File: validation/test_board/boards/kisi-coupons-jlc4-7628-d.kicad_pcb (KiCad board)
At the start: 4 copper layers, 50 x 96 mm, 19 parts, among them J1 292-04A-14, J10 292-04A-14, J11 292-04A-14, J12 292-04A-14, J13 292-04A-14, J14 292-04A-14, J15 292-04A-14, J16 292-04A-14, J2 292-04A-14, J3 292-04A-14, J4 292-04A-14, J5 292-04A-14, J6 292-04A-14, J7 292-04A-14, J8 292-04A-14, J9 292-04A-14

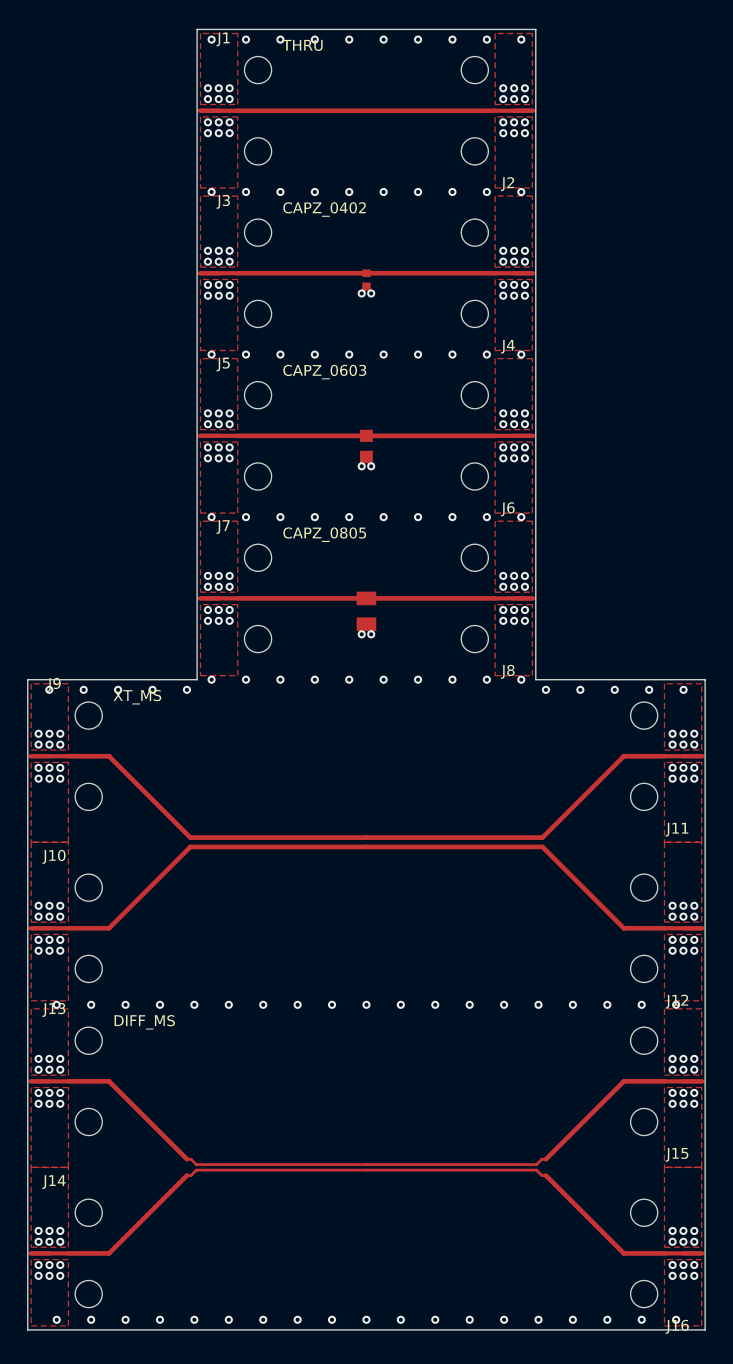
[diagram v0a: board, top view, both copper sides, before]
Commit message: Measurement coupons v3: Samtec 2.92 mm edge launch, 40 GHz plan
- Connector: Samtec 292-J-P-EP-ST-EL-01 (2.92 mm to 40 GHz, compression
  mount, PCB 1.02-2.54 mm; maintainer's decision 2026-10-30 on the RF
  group's advice) replaces the SMA Southwest 292-04A-14. Data, sources,
  the meaning of every footprint dimension of Samtec's drawing and the
  benchmark of Samtec's RF report (2023-06-01) in connectors.json.
- Footprint generated by make_coupons.py from parameters (Samtec's
  files are not committed: their terms forbid redistributing the
  models): geometry from drawing 292-J-P-EP-ST-EL-01-X-MKT rev C,
  plated screw holes 2.79 mm from the edge, +-2.92 mm, ground pads on
  top and bottom copper, signal tip 0.23 mm; marked DRAFT. The
  generator checks that no other net lies under the pads.
- Launch parametric (tip, taper, pad, coplanar section, ground cut,
  fence); default our 50 ohm coplanar launch inside the Samtec pads.
  --launch-cases writes kisi-fdtd cases; first runs (board side only)
  in fdtd_ref/launch_jlc4_7628: -18.9 dB worst to 40 GHz with the
  launch width to the edge, Samtec's 0.52 mm pad -14.6 dB.
- 40 GHz plan: stub notches of 6-layer VLV_L3 and 8-layer VLV_L6 now in
  the band, row via walls 2.54 -> 1.27 mm, measurement plan and ordering
  checklist to 40 GHz with 2.92 mm calibration and tools.
- Boards, manifests and 3D cases regenerated (widths unchanged); DRC
  with KiCad 7 on converted copies: no errors; kisi check rerun with
  kisi 0.3.1 (three v2 findings resolved in kisi since).

Co-Authored-By: Claude Opus 5.5 <noreply@anthropic.com>
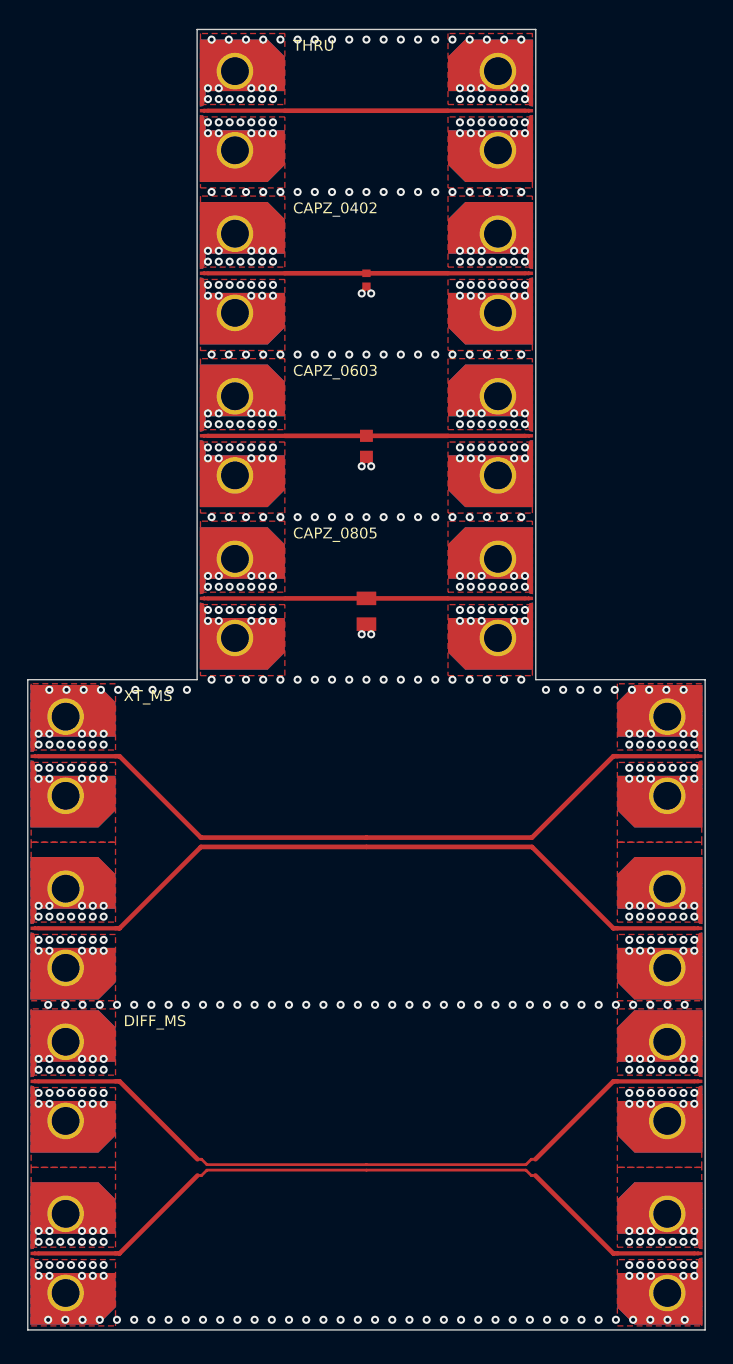
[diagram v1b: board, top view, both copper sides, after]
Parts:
- removed the J12 at (80.0, 96.3)
- added C1: 100nF 16V X7R, Capacitor_SMD:C_0402_1005Metric, F.Cu at (55.0, 48.5)
- J1, J10, J11, J13, J14, J15, J16, J2, J3, J4, J5, J6, J7, J8, J9: value 292-04A-14 -> 292-J-P-EP-ST-EL-01; footprint kisi_coupons:SWM_292-04A-14_EndLaunch_PLACEHOLDER -> kisi_coupons:Samtec_292-J-P-EP-ST-EL-01_EdgeLaunch
- J12: renamed from C1; value 100nF 16V X7R -> 292-J-P-EP-ST-EL-01; footprint Capacitor_SMD:C_0402_1005Metric -> kisi_coupons:Samtec_292-J-P-EP-ST-EL-01_EdgeLaunch
- moved J12 54.0 mm to (80.0, 96.3), turned to 180 degrees
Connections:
- J12 pad 1: SE_CAPZ_0402 -> SE_XT_V
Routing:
- net DP_DIFF_MS_P: track 54.7 -> 53.5 mm
- net DP_DIFF_MS_N: track 54.7 -> 53.5 mm
- net SE_XT_V: track 54.6 -> 53.4 mm
- net SE_XT_A: track 54.6 -> 53.4 mm
- net SE_THRU: track 24.6 -> 23.4 mm
- net SE_CAPZ_0805: track 24.6 -> 23.4 mm
- net SE_CAPZ_0603: track 24.6 -> 23.4 mm
- net SE_CAPZ_0402: track 24.6 -> 23.4 mm
- net GND: vias 296 -> 579
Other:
- board text added: "2026-10-30"
- board text added: "Connector footprint generated from Samtec's drawing (DRAFT, connectors.json); launch not yet optimised."
- board text added: "Copper comes to 0.2 mm from the left/right edges at the 2.92 mm edge launches (Samtec 292-J-P-EP-ST-EL-01, plated screw holes)."
- board text added: "JLC04161H-7628 v3"
- board text added: "kisi-coupons-jlc4-7628-d: kisi measurement coupons v3 (2026-10-30)"
- board text removed: "Connector footprint is a PLACEHOLDER (connectors.json) until the vendor drawing is supplied."
- board text removed: "Copper comes to 0.2 mm from the left/right edges at the SMA end launches (Southwest Microwave 292-04A-14)."
- board text removed: "JLC04161H-7628 v2 2026-10-22"
- board text removed: "kisi-coupons-jlc4-7628-d: kisi measurement coupons v2 (2026-10-22)"

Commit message: Launch optimisation step 1: launch width to the edge, fence 0.55 mm
- kisi-fdtd launch cases on the 7628 stack, board side (the connector's
  coax not modelled): our 50 ohm coplanar launch run to the edge with a
  0.55 mm fence from 0.5 mm gives |S11| -21.0 dB at worst to 40 GHz;
  the 0.8 mm draft fence left |S21| dips at 25-38 GHz (-18.9 dB),
  Samtec's 0.23 mm tip -15.7 dB (-16.8 dB with the pin modelled), its
  0.52 mm pad -14.6 dB. These become the defaults in connectors.json;
  the variants are named after what they change, results in
  fdtd_ref/launch_jlc4_7628. The jaw case is still not valid.
- Boards regenerated with the new launch (DRC with KiCad 7: no errors),
  kisi check rerun.
- The connector is in stock at DigiKey (maintainer): the boards set the
  timeline.

Co-Authored-By: Claude Opus 5.5 <noreply@anthropic.com>
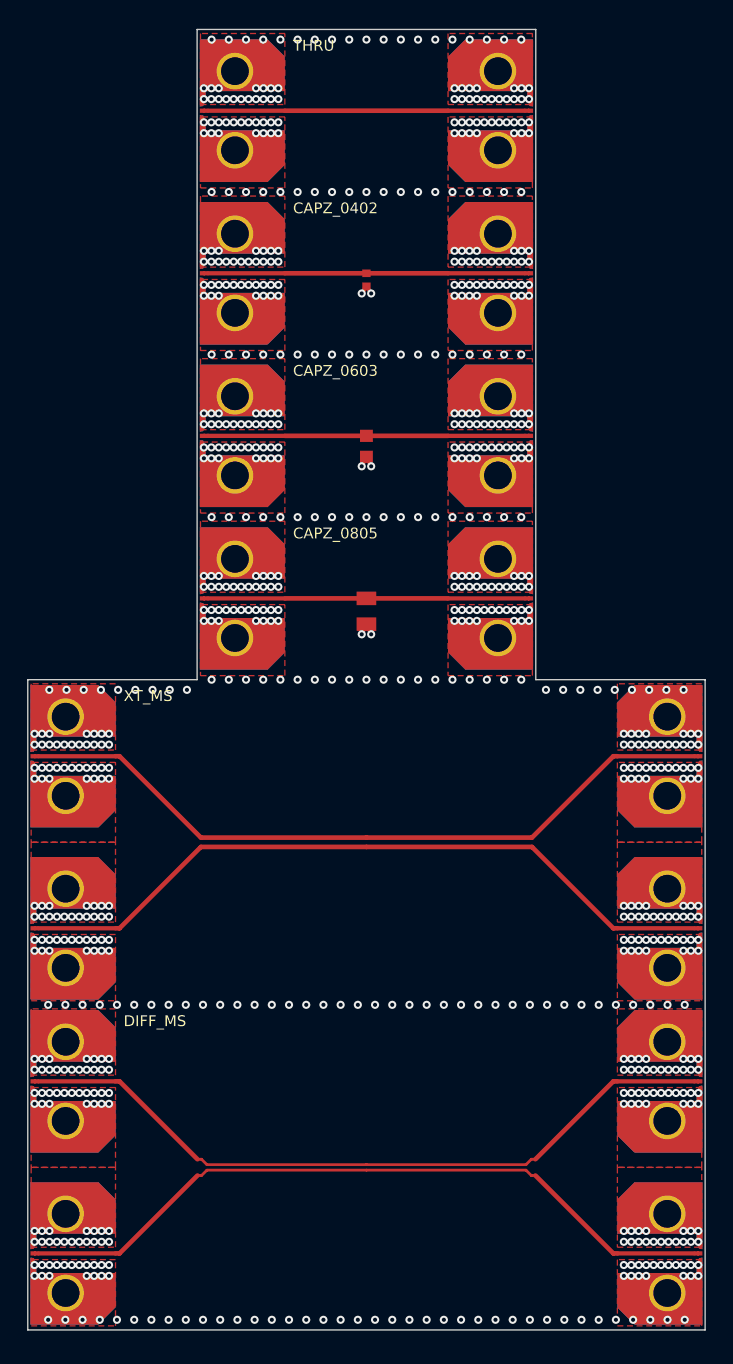
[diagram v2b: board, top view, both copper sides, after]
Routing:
- net GND: vias 579 -> 771
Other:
- board text added: "Connector footprint generated from Samtec's drawing (DRAFT, connectors.json); launch from a first kisi-fdtd optimisation step."
- board text removed: "Connector footprint generated from Samtec's drawing (DRAFT, connectors.json); launch not yet optimised."

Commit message: Coupon boards: own zone priorities, project-local footprint library
- KiCad 8/9 DRC reported overlapping zones of equal priority (the GND
  pour rectangles on L1 meet at 4-port launch pairs and along the CPWG
  coupons: 78 pairs on 26 boards). Every zone now has its own priority
  (planes 0, pours 1, 2, ..., islands and patches above); an outline
  check finds no equal-priority overlap left.
- The footprints the boards use are written as a project-local library
  (boards/kisi_coupons.pretty + fp-lib-table with ${KIPRJMOD}): the
  Samtec launch per launch width, the capacitor land patterns, the IC
  pin fields; per-instance Port/Status fields dropped, so board and
  library match. DRC (KiCad 7 on converted copies, with the library):
  no library warnings, no errors; the first-order boards are clean.
- Boards regenerated, kisi check unchanged.

Co-Authored-By: Claude Opus 5.5 <noreply@anthropic.com>
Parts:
- removed the C1 at (55.0, 48.5)
- removed the J9 at (30.0, 83.7)
- added J15: 292-J-P-EP-ST-EL-01, kisi_coupons:Samtec_292-J-P-EP-ST-EL-01_EdgeLaunch_W0.315, F.Cu at (80.0, 107.7)
- added J8: 292-J-P-EP-ST-EL-01, kisi_coupons:Samtec_292-J-P-EP-ST-EL-01_EdgeLaunch_W0.315, F.Cu at (67.5, 72.0)
- C1: renamed from J15; value 292-J-P-EP-ST-EL-01 -> 100nF 16V X7R; footprint kisi_coupons:Samtec_292-J-P-EP-ST-EL-01_EdgeLaunch -> kisi_coupons:C_0402_1005Metric_V
- C2: footprint Capacitor_SMD:C_0603_1608Metric -> kisi_coupons:C_0603_1608Metric_V
- C3: footprint Capacitor_SMD:C_0805_2012Metric -> kisi_coupons:C_0805_2012Metric_V
- J1, J10, J11, J12, J13, J14, J16, J2, J3, J4, J5, J6, J7: footprint kisi_coupons:Samtec_292-J-P-EP-ST-EL-01_EdgeLaunch -> kisi_coupons:Samtec_292-J-P-EP-ST-EL-01_EdgeLaunch_W0.315
- J9: renamed from J8; footprint kisi_coupons:Samtec_292-J-P-EP-ST-EL-01_EdgeLaunch -> kisi_coupons:Samtec_292-J-P-EP-ST-EL-01_EdgeLaunch_W0.315
- moved C1 64.2 mm to (55.0, 48.5), turned to 0 degrees
- moved J9 39.3 mm to (30.0, 83.7), turned to 0 degrees
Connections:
- C1 pad 1: DP_DIFF_MS_P -> SE_CAPZ_0402
- J9 pad 1: SE_CAPZ_0805 -> SE_XT_A
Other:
- board text added: "2026-10-31"
- board text added: "kisi-coupons-jlc4-7628-d: kisi measurement coupons v3 (2026-10-31)"
- board text removed: "2026-10-30"
- board text removed: "kisi-coupons-jlc4-7628-d: kisi measurement coupons v3 (2026-10-30)"
